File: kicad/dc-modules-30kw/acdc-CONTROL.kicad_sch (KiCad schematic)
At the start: 29 parts

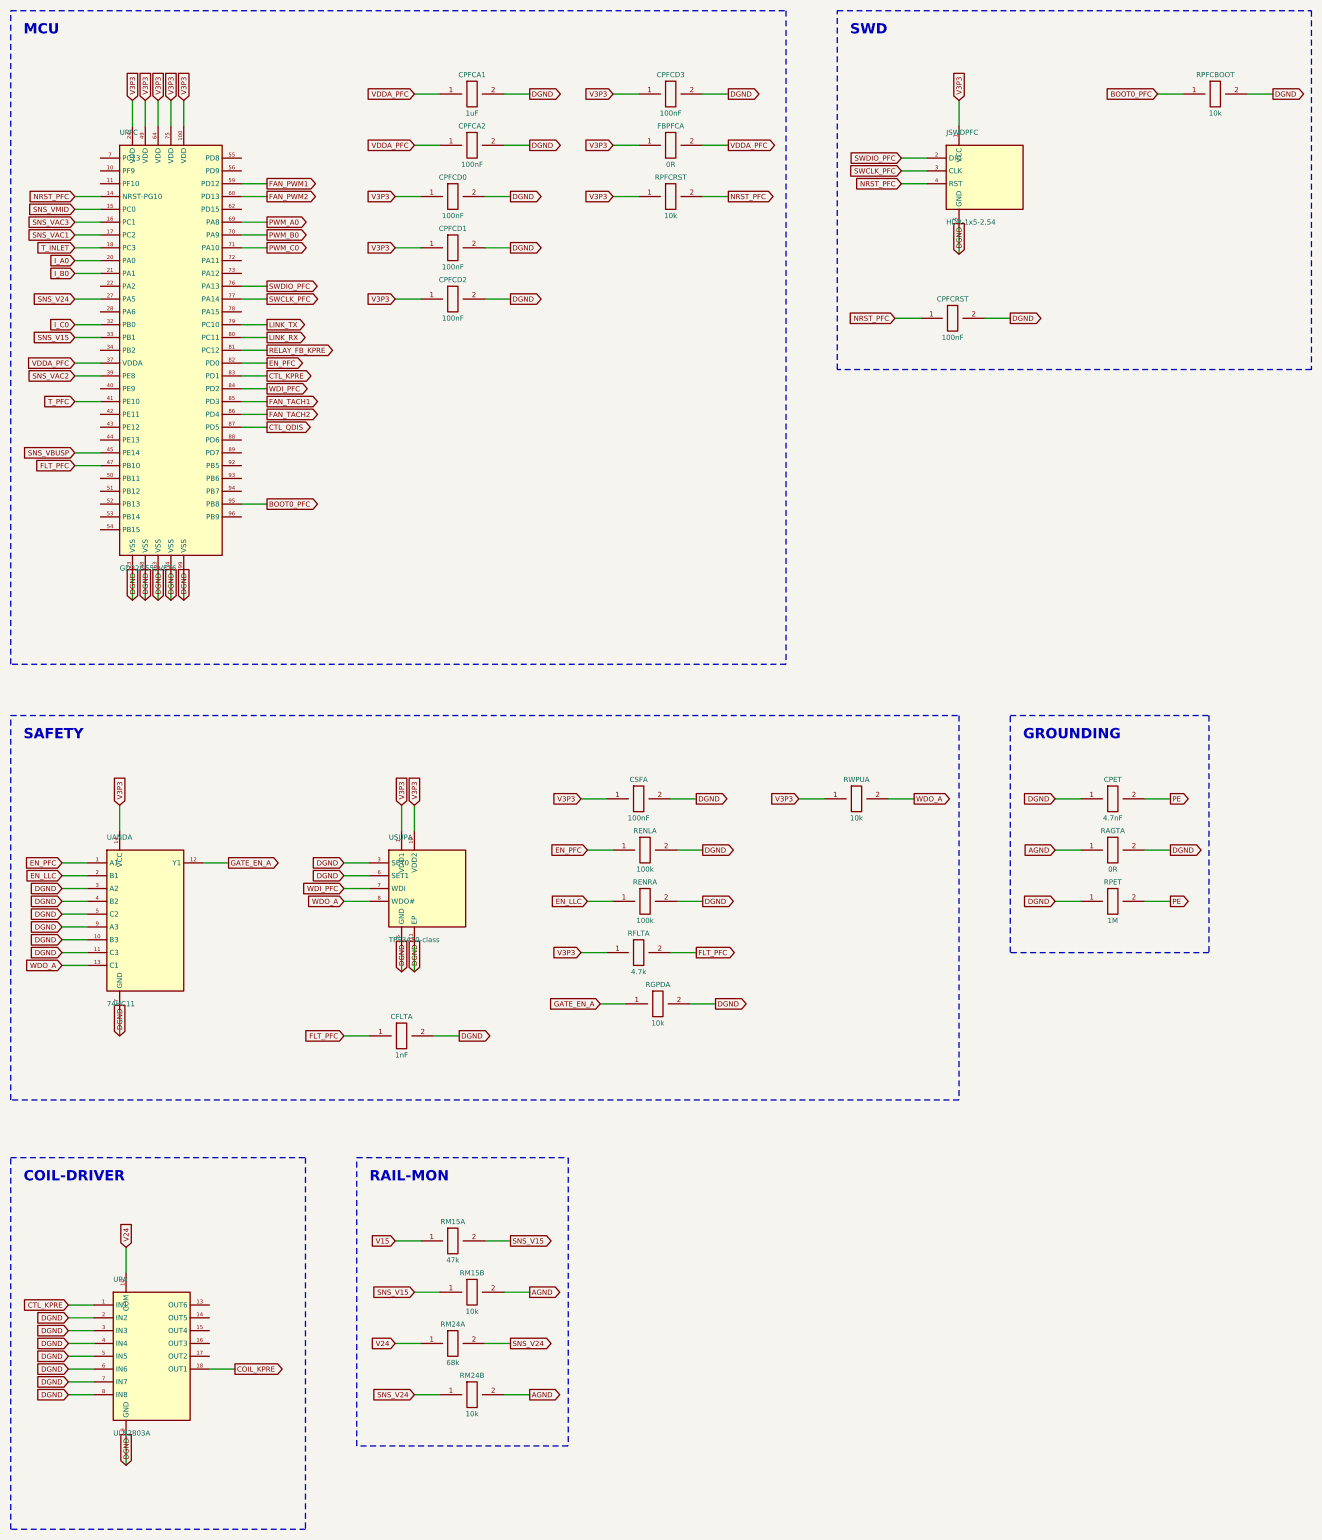
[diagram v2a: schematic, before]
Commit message: Visual pass on the hand-placed sheets: four draughting defects fixed
End-to-end inspection at zoom found four things the wide view hides:

1. The reference designator collided with the first top pin's number on
   every multi-pin IC. The library default had been moved but the INSTANCE
   property is what renders -- fixed there, right-justified clear of the body.
2. Power pins on the top/bottom edges drew their name INSIDE the body,
   rotated, straight through the first left/right pin name (VDD over PC13 on
   the MCU). Their names are now suppressed; the net label outside already
   says V3P3 / DGND, which is standard practice on a large MCU.
3. Unbound symbol pins rendered as bare stubs that read as unfinished
   connections. Every one now carries an explicit no-connect marker.
4. Single-pin parts (M8 studs, heatsink tab) were drawn by the IC path as
   large empty rectangles. They now use a real terminal symbol -- a small
   open circle on a stub -- in both the KiCad 10 and legacy generators.

Both verifiers still 100.00% (1735/1735 pins, 608 components, 0 floating
labels, 0 overlapping symbols, 0 unclosed frames). Page PDFs and the EasyEDA
import bundle regenerated against the corrected MCU pin map.

Co-Authored-By: Claude Fable 5 <noreply@anthropic.com>
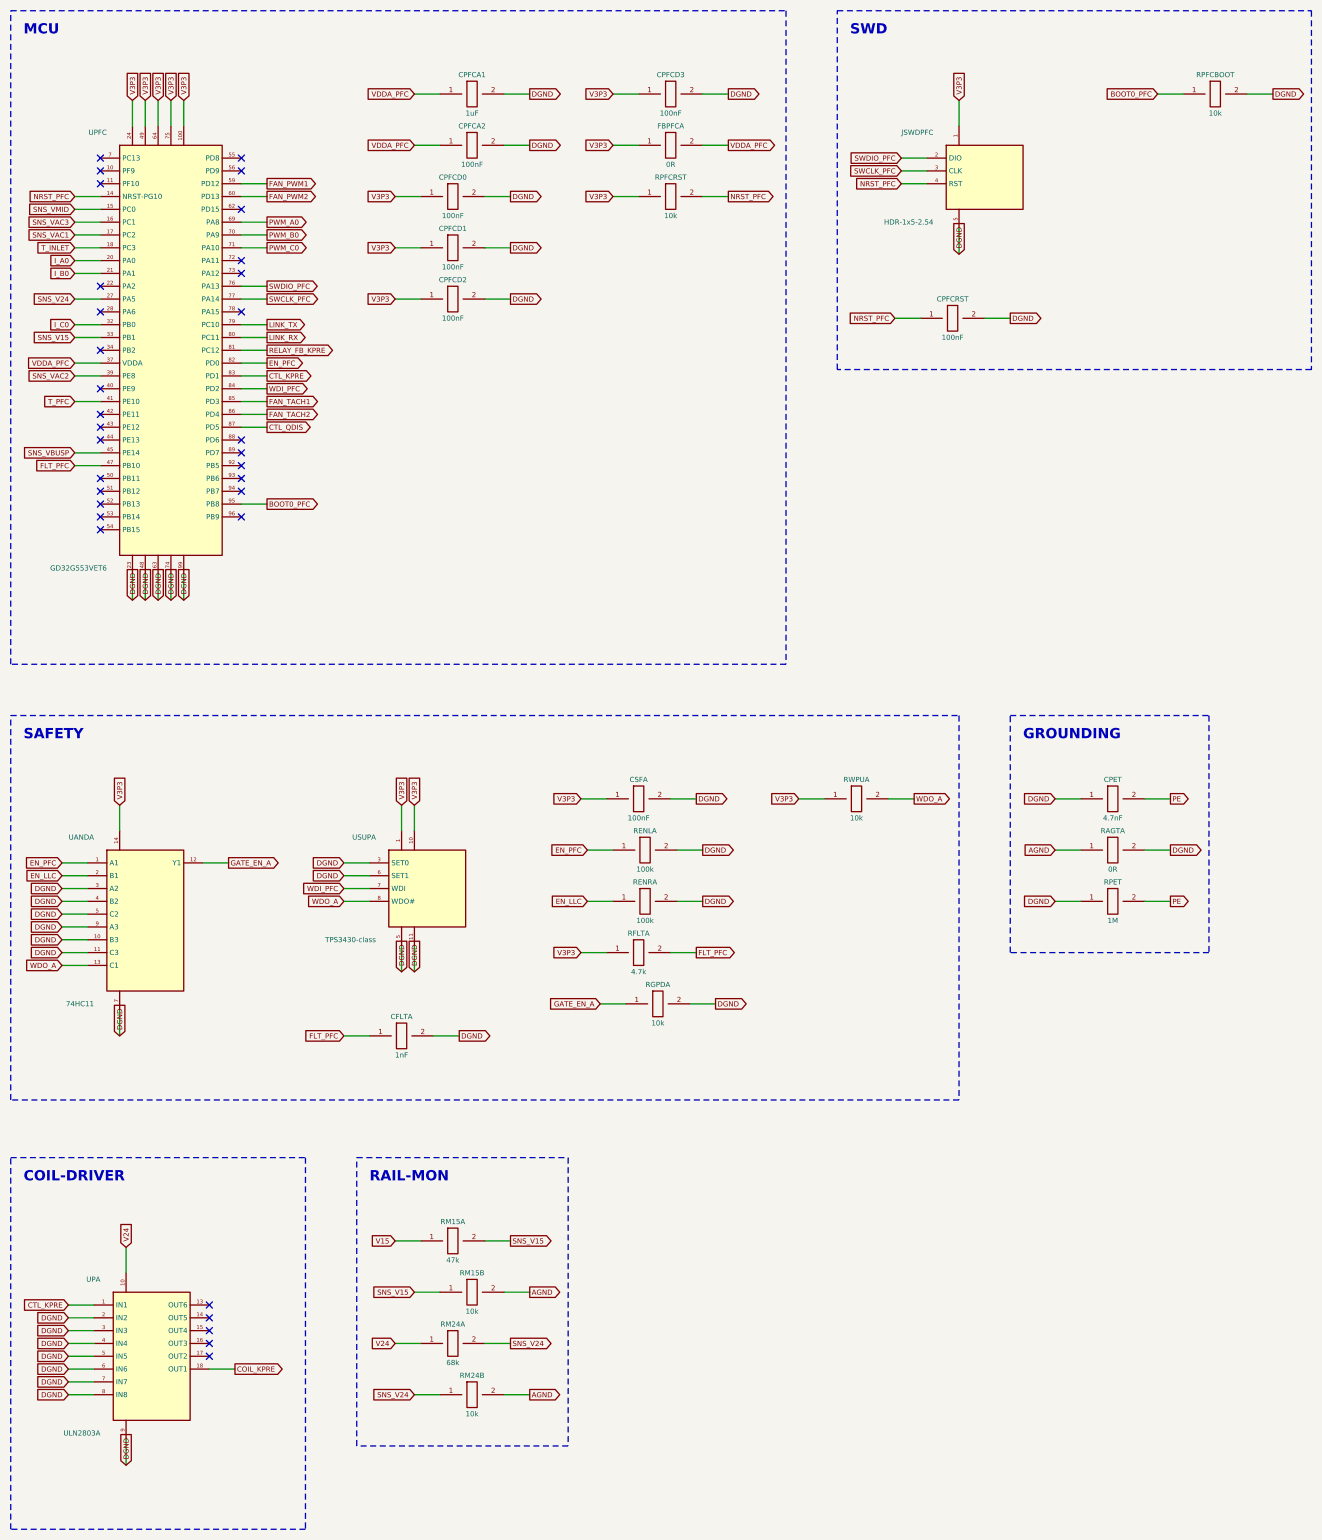
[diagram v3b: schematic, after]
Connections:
- no-connect marks 0 -> 32
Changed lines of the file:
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@@
 	(symbol (lib_id "dc-modules:GD32G553VET6") (at 44.45 80.01 0) (unit 1)
 		(exclude_from_sim no) (in_bom yes) (on_board yes) (dnp no)
-		(property "Reference" "UPFC" (at 34.29 36.83 0) (effects (font (size 1.016 1.016)) (justify left)))
-		(property "Value" "GD32G553VET6" (at 34.29 123.19 0) (effects (font (size 1.016 1.016)) (justify left)))
+		(property "Reference" "UPFC" (at 31.75 36.83 0) (effects (font (size 1.016 1.016)) (justify right)))
+		(property "Value" "GD32G553VET6" (at 31.75 123.19 0) (effects (font (size 1.016 1.016)) (justify right)))
 		(property "LCSC" "" (at 44.45 80.01 0) (effects (font (size 1.016 1.016)) (hide yes)))
 		(instances (project "dc-modules-30kw" (path "/97ccdda6-cbe2-4ab6-a01c-6e85c07d27c9" (reference "UPFC") (unit 1)))))
+	(no_connect (at 30.48 41.910000000000004))
+	(no_connect (at 30.48 44.45))
+	(no_connect (at 30.48 46.99))
 	(wire (pts (xy 30.48 49.53) (xy 25.4 49.53)) (stroke (width 0) (type default)))
 	(global_label "NRST_PFC" (shape input) (at 25.4 49.53 180)
@@
 	(global_label "I_B0" (shape input) (at 25.4 64.77 180)
 		(effects (font (size 1.016 1.016)) (justify right)))
+	(no_connect (at 30.48 67.31))
 	(wire (pts (xy 30.48 69.85) (xy 25.4 69.85)) (stroke (width 0) (type default)))
 	(global_label "SNS_V24" (shape input) (at 25.4 69.85 180)
 		(effects (font (size 1.016 1.016)) (justify right)))
+	(no_connect (at 30.48 72.39))
 	(wire (pts (xy 30.48 74.93) (xy 25.4 74.93)) (stroke (width 0) (type default)))
 	(global_label "I_C0" (shape input) (at 25.4 74.93 180)
@@
 	(global_label "SNS_V15" (shape input) (at 25.4 77.47 180)
 		(effects (font (size 1.016 1.016)) (justify right)))
+	(no_connect (at 30.48 80.01))
 	(wire (pts (xy 30.48 82.55) (xy 25.4 82.55)) (stroke (width 0) (type default)))
 	(global_label "VDDA_PFC" (shape input) (at 25.4 82.55 180)
@@
 	(global_label "SNS_VAC2" (shape input) (at 25.4 85.09 180)
 		(effects (font (size 1.016 1.016)) (justify right)))
+	(no_connect (at 30.48 87.63))
 	(wire (pts (xy 30.48 90.17) (xy 25.4 90.17)) (stroke (width 0) (type default)))
 	(global_label "T_PFC" (shape input) (at 25.4 90.17 180)
 		(effects (font (size 1.016 1.016)) (justify right)))
+	(no_connect (at 30.48 92.71000000000001))
+	(no_connect (at 30.48 95.25))
+	(no_connect (at 30.48 97.79))
 	(wire (pts (xy 30.48 100.33) (xy 25.4 100.33)) (stroke (width 0) (type default)))
 	(global_label "SNS_VBUSP" (shape input) (at 25.4 100.33 180)
@@
 	(global_label "FLT_PFC" (shape input) (at 25.4 102.87 180)
 		(effects (font (size 1.016 1.016)) (justify right)))
+	(no_connect (at 30.48 105.41))
+	(no_connect (at 30.48 107.95))
+	(no_connect (at 30.48 110.49))
+	(no_connect (at 30.48 113.03))
+	(no_connect (at 30.48 115.57000000000001))
+	(no_connect (at 58.42 41.910000000000004))
+	(no_connect (at 58.42 44.45))
 	(wire (pts (xy 58.42 46.99) (xy 63.5 46.99)) (stroke (width 0) (type default)))
 	(global_label "FAN_PWM1" (shape output) (at 63.5 46.99 0)
@@
 	(global_label "FAN_PWM2" (shape output) (at 63.5 49.53 0)
 		(effects (font (size 1.016 1.016)) (justify left)))
+	(no_connect (at 58.42 52.07))
 	(wire (pts (xy 58.42 54.61) (xy 63.5 54.61)) (stroke (width 0) (type default)))
 	(global_label "PWM_A0" (shape output) (at 63.5 54.61 0)
@@
 	(global_label "PWM_C0" (shape output) (at 63.5 59.69 0)
 		(effects (font (size 1.016 1.016)) (justify left)))
+	(no_connect (at 58.42 62.230000000000004))
+	(no_connect (at 58.42 64.77))
 	(wire (pts (xy 58.42 67.31) (xy 63.5 67.31)) (stroke (width 0) (type default)))
 	(global_label "SWDIO_PFC" (shape output) (at 63.5 67.31 0)
@@
 	(global_label "SWCLK_PFC" (shape output) (at 63.5 69.85 0)
 		(effects (font (size 1.016 1.016)) (justify left)))
+	(no_connect (at 58.42 72.39))
 	(wire (pts (xy 58.42 74.93) (xy 63.5 74.93)) (stroke (width 0) (type default)))
 	(global_label "LINK_TX" (shape output) (at 63.5 74.93 0)
@@
 	(global_label "CTL_QDIS" (shape output) (at 63.5 95.25 0)
 		(effects (font (size 1.016 1.016)) (justify left)))
+	(no_connect (at 58.42 97.79))
+	(no_connect (at 58.42 100.33))
+	(no_connect (at 58.42 102.87))
+	(no_connect (at 58.42 105.41))
+	(no_connect (at 58.42 107.95))
 	(wire (pts (xy 58.42 110.49) (xy 63.5 110.49)) (stroke (width 0) (type default)))
 	(global_label "BOOT0_PFC" (shape output) (at 63.5 110.49 0)
 		(effects (font (size 1.016 1.016)) (justify left)))
+	(no_connect (at 58.42 113.03))
 	(wire (pts (xy 36.83 35.56) (xy 36.83 30.48)) (stroke (width 0) (type default)))
 	(global_label "V3P3" (shape input) (at 36.83 30.48 90)
@@
 	(symbol (lib_id "dc-modules:HDR-1x5-2.54") (at 205.74 45.72 0) (unit 1)
 		(exclude_from_sim no) (in_bom yes) (on_board yes) (dnp no)
-		(property "Reference" "JSWDPFC" (at 198.12 36.83 0) (effects (font (size 1.016 1.016)) (justify left)))
-		(property "Value" "HDR-1x5-2.54" (at 198.12 54.61 0) (effects (font (size 1.016 1.016)) (justify left)))
+		(property "Reference" "JSWDPFC" (at 195.58 36.83 0) (effects (font (size 1.016 1.016)) (justify right)))
+		(property "Value" "HDR-1x5-2.54" (at 195.58 54.61 0) (effects (font (size 1.016 1.016)) (justify right)))
 		(property "LCSC" "" (at 205.74 45.72 0) (effects (font (size 1.016 1.016)) (hide yes)))
 		(instances (project "dc-modules-30kw" (path "/97ccdda6-cbe2-4ab6-a01c-6e85c07d27c9" (reference "JSWDPFC") (unit 1)))))
@@
 	(symbol (lib_id "dc-modules:74HC11") (at 39.37 193.04 0) (unit 1)
 		(exclude_from_sim no) (in_bom yes) (on_board yes) (dnp no)
-		(property "Reference" "UANDA" (at 31.75 176.53 0) (effects (font (size 1.016 1.016)) (justify left)))
-		(property "Value" "74HC11" (at 31.75 209.55 0) (effects (font (size 1.016 1.016)) (justify left)))
+		(property "Reference" "UANDA" (at 29.21 176.53 0) (effects (font (size 1.016 1.016)) (justify right)))
+		(property "Value" "74HC11" (at 29.21 209.55 0) (effects (font (size 1.016 1.016)) (justify right)))
 		(property "LCSC" "" (at 39.37 193.04 0) (effects (font (size 1.016 1.016)) (hide yes)))
 		(instances (project "dc-modules-30kw" (path "/97ccdda6-cbe2-4ab6-a01c-6e85c07d27c9" (reference "UANDA") (unit 1)))))
@@
 	(symbol (lib_id "dc-modules:TPS3430-class") (at 95.25 186.69 0) (unit 1)
 		(exclude_from_sim no) (in_bom yes) (on_board yes) (dnp no)
-		(property "Reference" "USUPA" (at 87.63 176.53 0) (effects (font (size 1.016 1.016)) (justify left)))
-		(property "Value" "TPS3430-class" (at 87.63 196.85 0) (effects (font (size 1.016 1.016)) (justify left)))
+		(property "Reference" "USUPA" (at 85.09 176.53 0) (effects (font (size 1.016 1.016)) (justify right)))
+		(property "Value" "TPS3430-class" (at 85.09 196.85 0) (effects (font (size 1.016 1.016)) (justify right)))
 		(property "LCSC" "" (at 95.25 186.69 0) (effects (font (size 1.016 1.016)) (hide yes)))
 		(instances (project "dc-modules-30kw" (path "/97ccdda6-cbe2-4ab6-a01c-6e85c07d27c9" (reference "USUPA") (unit 1)))))
@@
 	(symbol (lib_id "dc-modules:ULN2803A") (at 40.64 279.4 0) (unit 1)
 		(exclude_from_sim no) (in_bom yes) (on_board yes) (dnp no)
-		(property "Reference" "UPA" (at 33.02 264.16 0) (effects (font (size 1.016 1.016)) (justify left)))
-		(property "Value" "ULN2803A" (at 33.02 294.64 0) (effects (font (size 1.016 1.016)) (justify left)))
+		(property "Reference" "UPA" (at 30.48 264.16 0) (effects (font (size 1.016 1.016)) (justify right)))
+		(property "Value" "ULN2803A" (at 30.48 294.64 0) (effects (font (size 1.016 1.016)) (justify right)))
 		(property "LCSC" "" (at 40.64 279.4 0) (effects (font (size 1.016 1.016)) (hide yes)))
 		(instances (project "dc-modules-30kw" (path "/97ccdda6-cbe2-4ab6-a01c-6e85c07d27c9" (reference "UPA") (unit 1)))))
@@
 	(global_label "DGND" (shape input) (at 24.13 287.02 180)
 		(effects (font (size 1.016 1.016)) (justify right)))
+	(no_connect (at 52.07 269.24))
+	(no_connect (at 52.07 271.78000000000003))
+	(no_connect (at 52.07 274.32))
+	(no_connect (at 52.07 276.86))
+	(no_connect (at 52.07 279.4))
 	(wire (pts (xy 52.07 281.94) (xy 57.15 281.94)) (stroke (width 0) (type default)))
 	(global_label "COIL_KPRE" (shape output) (at 57.15 281.94 0)
